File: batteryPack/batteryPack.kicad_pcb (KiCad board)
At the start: 2 copper layers, 204 x 78 mm, 48 parts, among them J1 Mirco USB, J10 B1+, J11 B1-, J12 B2-, J13 B1+, J14 B1-, J15 B2+, J16 B2-, J2 B1+, J3 B1-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

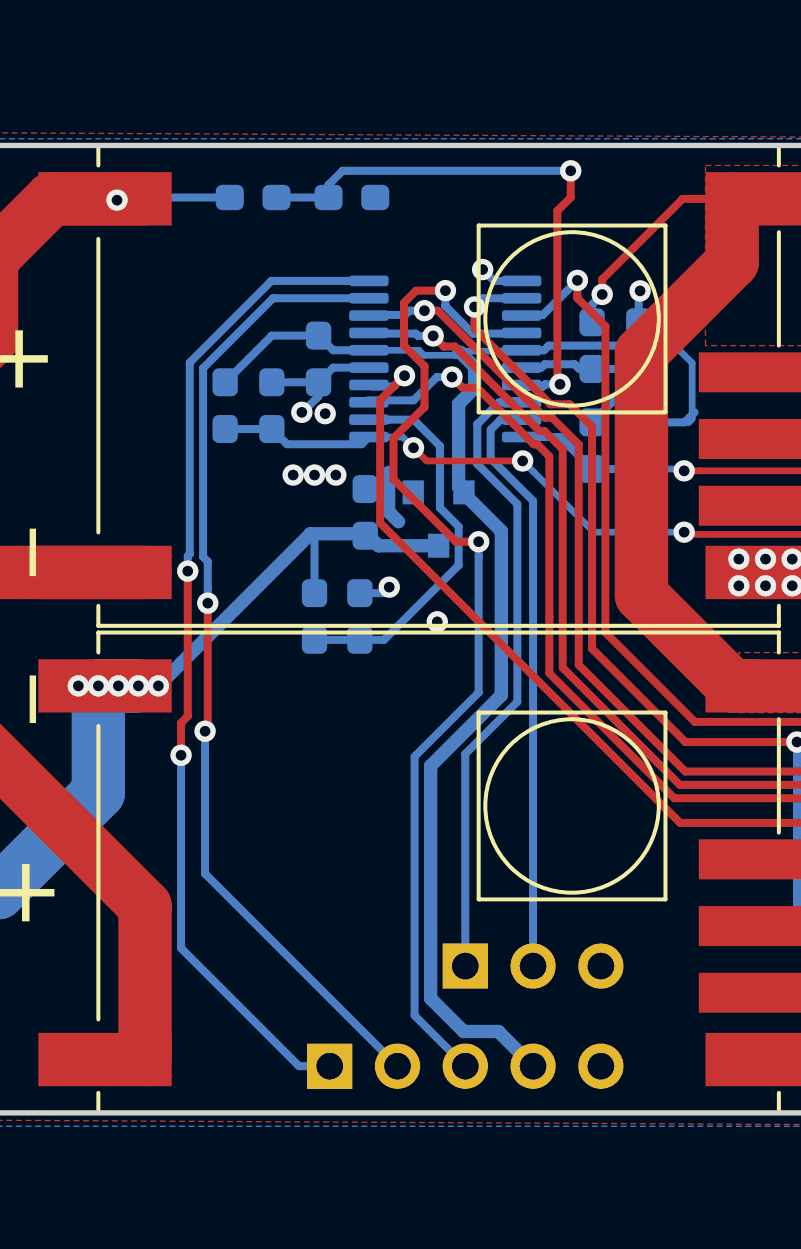
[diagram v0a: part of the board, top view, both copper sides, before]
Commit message: Make room for mouse bites
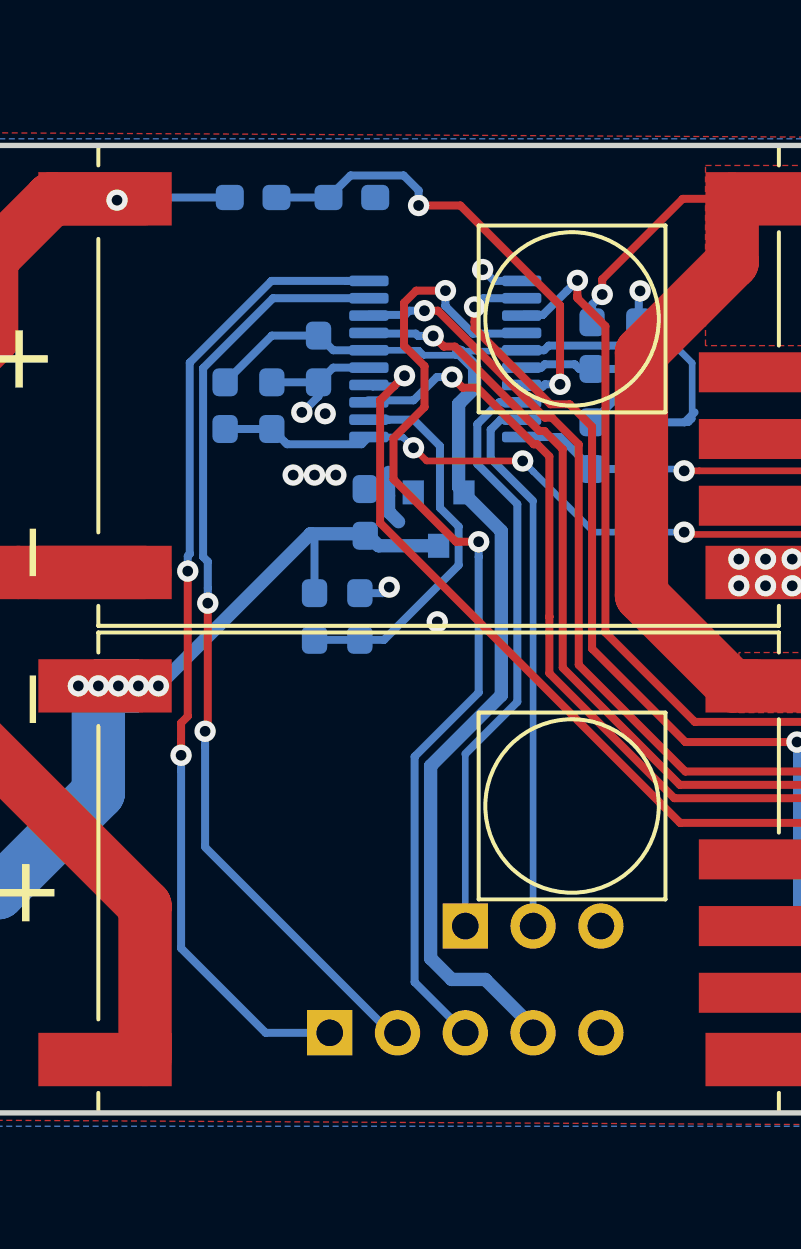
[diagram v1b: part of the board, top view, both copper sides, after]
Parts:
- moved J8 1.50 mm to (209.5, 81.2)
- moved J7 1.25 mm to (204.4, 85.2)
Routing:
- net BAT1_V: track 21.5 -> 17.8 mm
- net TX: track 23.7 -> 22.2 mm
- net RX: track 22.1 -> 20.6 mm
- net SWDIO: track 36.6 -> 35.2 mm
- net +3V3: track 53.4 -> 52.1 mm
- net RST: track 38.7 -> 37.5 mm
- net SWCLK: track 37.5 -> 36.8 mm

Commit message: Bump version on silkscreen to 1.0
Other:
- board text added: "RB0002 Battery Pack Battery Board v1.0 06/2020 CC BY-SA 4.0 github.com/RoboticsBrno/RB0002-BatteryPack"
- board text added: "RB0002 Battery Pack Charger v1.0 06/2020"
- board text added: "RB0002 Battery Pack Connector v1.0"
- board text removed: "RB0002 Battery Pack Battery Board v0.1 04/2020 CC BY-SA 4.0 github.com/RoboticsBrno/RB0002-BatteryPack"
- board text removed: "RB0002 Battery Pack Charger v0.1 04/2020"
- board text removed: "RB0002 Battery Pack Connector v0.1"
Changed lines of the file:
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@@
     (effects (font (size 2 2) (thickness 0.4)) (justify mirror))
   )
-  (gr_text "RB0002 Battery Pack\nCharger\n v0.1 04/2020" (at 221.49 69.91 270) (layer B.SilkS)
+  (gr_text "RB0002 Battery Pack\nCharger\n v1.0 06/2020" (at 221.49 69.91 270) (layer B.SilkS)
     (effects (font (size 1.5 1.5) (thickness 0.3)) (justify mirror))
   )
@@
     (effects (font (size 1.3 1.3) (thickness 0.2)))
   )
-  (gr_text "RB0002 Battery Pack\nConnector       v0.1" (at 125 69.75 270) (layer B.SilkS)
+  (gr_text "RB0002 Battery Pack\nConnector       v1.0" (at 125 69.75 270) (layer B.SilkS)
     (effects (font (size 1.5 1.5) (thickness 0.3)) (justify mirror))
   )
@@
   (gr_arc (start 31 108) (end 30 108) (angle -90) (layer Edge.Cuts) (width 0.2))
   (gr_arc (start 69 108) (end 69 109) (angle -90) (layer Edge.Cuts) (width 0.2))
-  (gr_text "RB0002 Battery Pack\nBattery Board\nv0.1     04/2020     CC BY-SA 4.0\ngithub.com/RoboticsBrno/RB0002-BatteryPack" (at 46 69 90) (layer F.SilkS)
+  (gr_text "RB0002 Battery Pack\nBattery Board\nv1.0     06/2020     CC BY-SA 4.0\ngithub.com/RoboticsBrno/RB0002-BatteryPack" (at 46 69 90) (layer F.SilkS)
     (effects (font (size 1.5 1.5) (thickness 0.3)))
   )
